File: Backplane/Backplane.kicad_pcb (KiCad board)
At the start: 4 copper layers, 101.6 x 120.6 mm, 40 parts, among them J10 Conn_01x02, J11 Conn_01x02, J12 Conn_02x12_Odd_Even, J13 Conn_01x02, J14 Conn_01x02, J15 Conn_01x02, J16 Conn_01x02, J17 Conn_01x02, J18 Conn_01x02, J19 Conn_01x02_Pin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

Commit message: Changed Backplane and Power Card for proper connection between the killswitches in the new system
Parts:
- added NJKS: Conn_01x02, Connector_JST:JST_PH_B2B-PH-K_1x02_P2.00mm_Vertical, F.Cu at (74.0, 137.0)
- J27: renamed from Power (+12V)
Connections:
- J1 pad A27: SW2 -> unconnected-(J1-PadA27)
- J1 pad A28: GND -> unconnected-(J1-PadA28)
- J1 pad B27: SW2 -> SW
- J1 pad B28: SW1 -> NJSW
- J1 pad C27: GND -> SW
- J1 pad C28: SW1 -> NJSW
- J9 pad 1: SW2 -> SW
- J9 pad 2: SW1 -> GND
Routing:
- net SW1: track 166.3 -> 0.00 mm, vias 1 -> 0
- net SW2: track 159.0 -> 0.00 mm, vias 1 -> 0
- net SW: track 0.00 -> 156.5 mm, vias 0 -> 1
- net NJSW: track 0.00 -> 155.3 mm, vias 0 -> 1

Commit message: Added short on power card and fixed some connections
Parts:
- renumbered J27 to 12V
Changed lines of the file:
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@@
 		(descr "JST PH series connector, B2B-PH-K (http://www.jst-mfg.com/product/pdf/eng/ePH.pdf), generated with kicad-footprint-generator")
 		(tags "connector JST PH vertical")
-		(property "Reference" "J27"
-			(at -2.5 -3 90)
+		(property "Reference" "12V"
+			(at -3 -2.5 90)
 			(layer "F.SilkS")
 			(effects
@@
 			(layer "F.Fab")
 		)
-		(fp_text user "${REFERENCE}"
-			(at 1 1.5 90)
-			(layer "F.Fab")
-			(effects
-				(font
-					(size 1 1)
-					(thickness 0.15)
-				)
-			)
-		)
 		(pad "1" thru_hole roundrect
 			(at 0 0 90)
@@
 			(layer "F.Fab")
 		)
-		(fp_text user "${REFERENCE}"
-			(at 1 1.5 90)
-			(layer "F.Fab")
-			(effects
-				(font
-					(size 1 1)
-					(thickness 0.15)
-				)
-			)
-		)
 		(pad "1" thru_hole roundrect

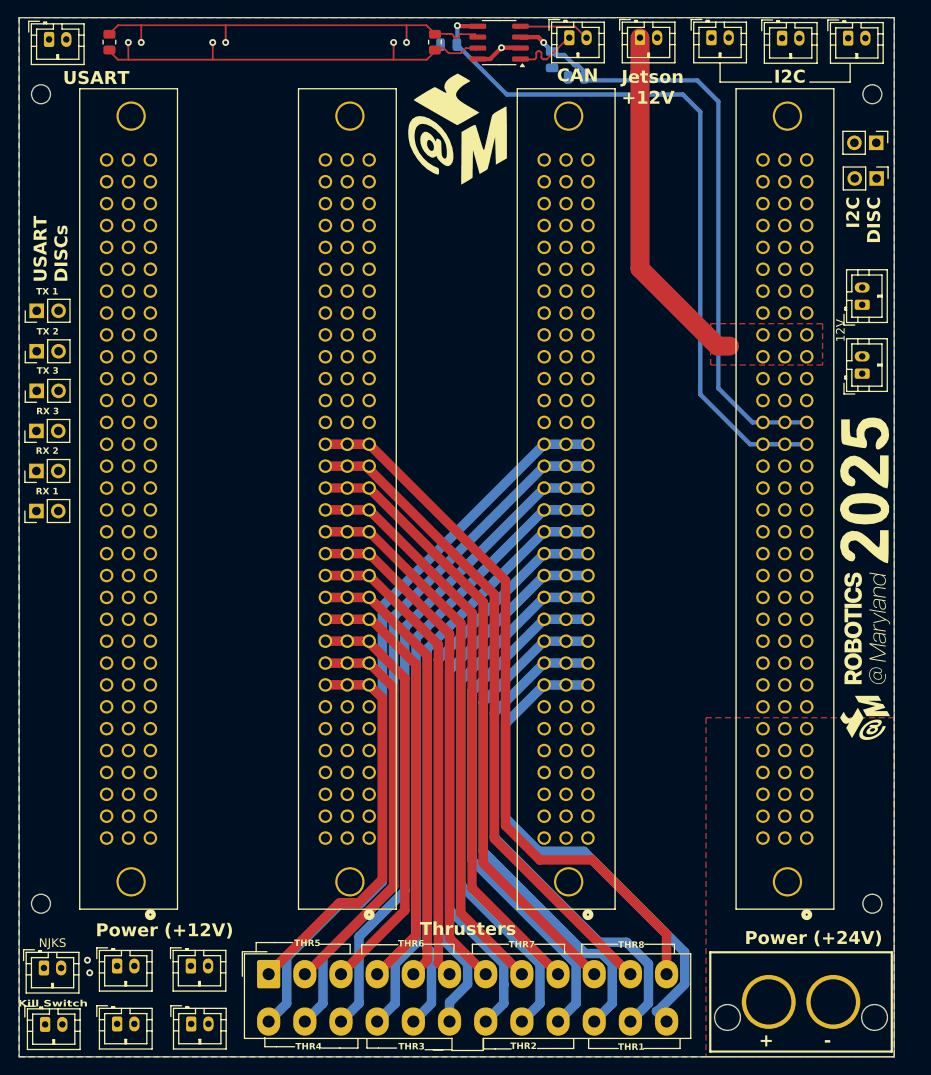
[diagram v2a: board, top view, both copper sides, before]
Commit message: Added Silkscreen & Backplane Integration
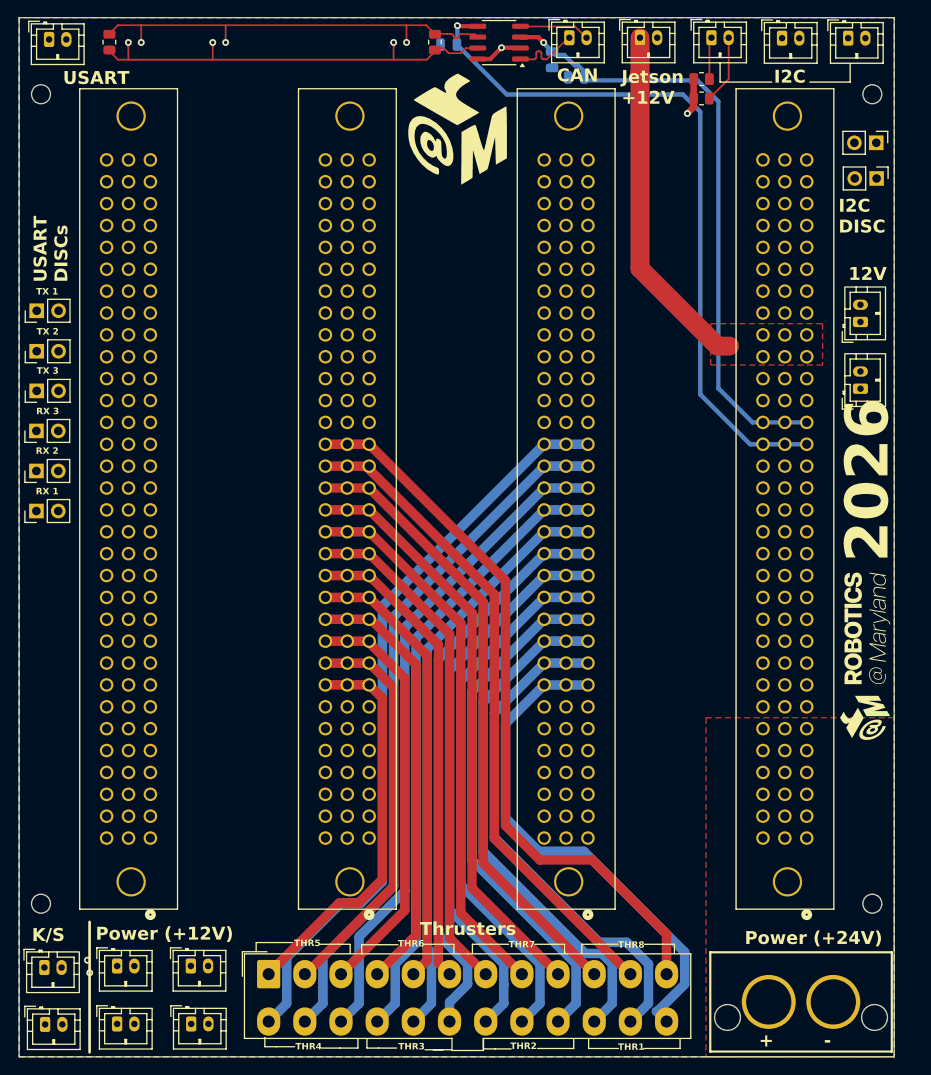
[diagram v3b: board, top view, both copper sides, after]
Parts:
- removed 12V, NJKS: Conn_01x02, Connector_JST:JST_PH_B2B-PH-K_1x02_P2.00mm_Vertical
- removed the G*** at (169.4, 81.5)
- added J27: Conn_01x02, Connector_JST:JST_PH_B2B-PH-K_1x02_P2.00mm_Vertical, F.Cu at (168.8, 69.8)
- added J28: Conn_01x02, Connector_JST:JST_PH_B2B-PH-K_1x02_P2.00mm_Vertical, F.Cu at (74.0, 136.9)
- added R3: 4.7k, Resistor_SMD:R_0805_2012Metric, F.Cu at (150.3, 33.8)
- added R4: 4.7k, Resistor_SMD:R_0805_2012Metric, F.Cu at (150.3, 36.0)
- moved J15 6.00 mm to (168.8, 62.0)
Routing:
- net +3.3V: track 0.00 -> 34.1 mm, vias 0 -> 1
- net I2CJetson-: track 45.6 -> 53.5 mm
- net I2CJetson+: track 45.6 -> 50.5 mm
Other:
- board text added: "12V"
- board text added: "2026"
- board text added: "K/S"
- board text removed: "Kill Switch"

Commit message: Kurt Changes
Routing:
- net +3.3V: track 34.1 -> 37.9 mm
- net 12V Jetson: track 40.9 -> 42.8 mm
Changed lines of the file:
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@@
+	)
+	(segment
+		(start 146.7 39.8)
+		(end 149.4375 37.0625)
+		(width 0.75)
+		(layer "F.Cu")
+		(net 5)
+	)
+	(segment
+		(start 146.7 59)
+		(end 146.7 39.8)
+		(width 0.75)
+		(layer "F.Cu")
+		(net 5)
 	)
 	(segment
@@
 	(segment
 		(start 149.4375 37.0625)
-		(end 148.7 37.8)
+		(end 149.4375 36.05)
 		(width 0.75)
 		(layer "F.Cu")
 		(net 5)
 	)
-	(segment
-		(start 149.4375 36.05)
-		(end 149.4375 37.0625)
-		(width 0.75)
-		(layer "F.Cu")
-		(net 5)
-	)
 	(via
-		(at 148.7 37.8)
+		(at 146.7 59)
 		(size 0.8)
 		(drill 0.4)
@@
 	)
 	(segment
-		(start 148.7 37.8)
-		(end 148.7 67.55)
+		(start 146.7 59)
+		(end 146.7 70.6)
 		(width 0.75)
 		(layer "In1.Cu")
@@
 	)
 	(segment
-		(start 143.2 55.8)
-		(end 151.6 64.2)
-		(width 2.2)
-		(layer "F.Cu")
-		(net 16)
-	)
-	(segment
-		(start 152.2 64.8)
+		(start 149 64.8)
 		(end 153.6 64.8)
 		(width 2.2)
@@
 	)
 	(segment
-		(start 151.6 64.2)
-		(end 152.2 64.8)
+		(start 143.2 29)
+		(end 143.2 59)
 		(width 2.2)
 		(layer "F.Cu")
@@
 	)
 	(segment
-		(start 143.2 29)
-		(end 143.2 33)
+		(start 143.2 59)
+		(end 149 64.8)
 		(width 2.2)
 		(layer "F.Cu")
-		(net 16)
-	)
-	(segment
-		(start 143.2 33)
-		(end 143.2 55.8)
-		(width 2.2)
-		(layer "F.Cu")

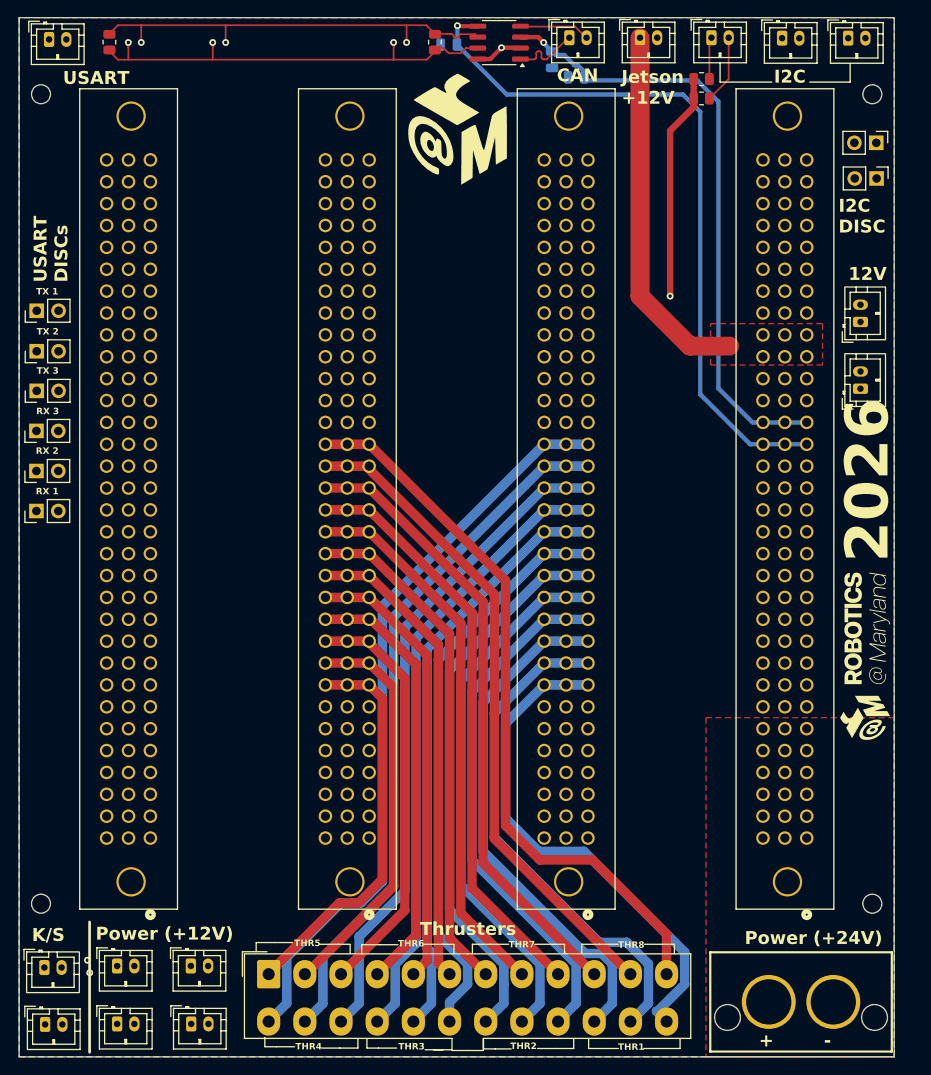
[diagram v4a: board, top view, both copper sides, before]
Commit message: Added More Connectors to Backplane
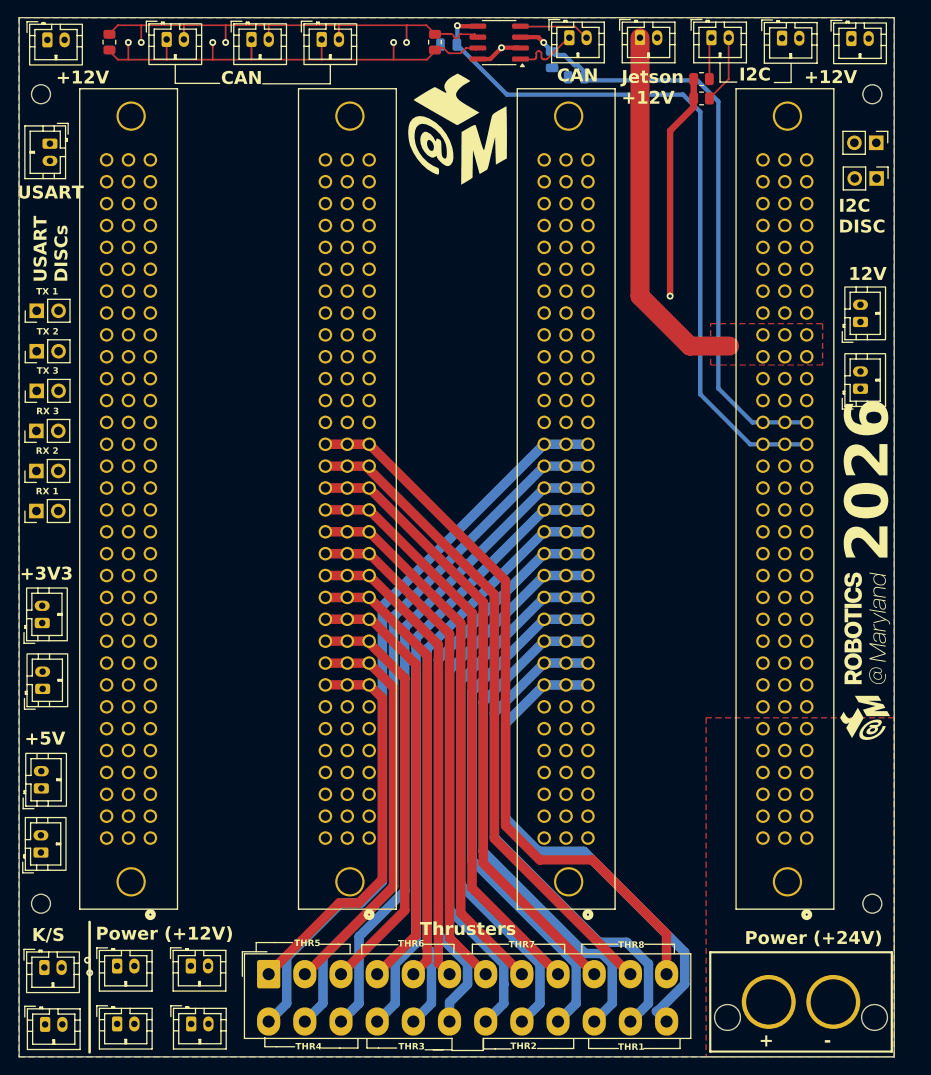
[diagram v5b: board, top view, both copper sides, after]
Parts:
- removed J16: Conn_01x02, Connector_JST:JST_PH_B2B-PH-K_1x02_P2.00mm_Vertical
- added J29: Conn_01x02, Connector_JST:JST_PH_B2B-PH-K_1x02_P2.00mm_Vertical, F.Cu at (88.2, 29.2)
- added J30: Conn_01x02, Connector_JST:JST_PH_B2B-PH-K_1x02_P2.00mm_Vertical, F.Cu at (98.1, 29.2)
- added J31: Conn_01x02, Connector_JST:JST_PH_B2B-PH-K_1x02_P2.00mm_Vertical, F.Cu at (73.8, 104.6)
- added J32: Conn_01x02, Connector_JST:JST_PH_B2B-PH-K_1x02_P2.00mm_Vertical, F.Cu at (73.8, 97.0)
- added J33: Conn_01x02, Connector_JST:JST_PH_B2B-PH-K_1x02_P2.00mm_Vertical, F.Cu at (73.7, 116.2)
- added J34: Conn_01x02, Connector_JST:JST_PH_B2B-PH-K_1x02_P2.00mm_Vertical, F.Cu at (73.7, 123.6)
- added J35: Conn_01x02, Connector_JST:JST_PH_B2B-PH-K_1x02_P2.00mm_Vertical, F.Cu at (106.2, 29.2)
- added J36: Conn_01x02, Connector_JST:JST_PH_B2B-PH-K_1x02_P2.00mm_Vertical, F.Cu at (74.4, 29.2)
- added J37: Conn_01x02, Connector_JST:JST_PH_B2B-PH-K_1x02_P2.00mm_Vertical, F.Cu at (167.8, 29.1)
- moved J18 12.1 mm to (74.7, 41.3), turned to -90 degrees
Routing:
- net USART+: track 56.5 -> 30.2 mm
- net I2CJetson+: track 50.5 -> 33.0 mm
- net I2CJetson-: track 53.5 -> 40.2 mm
- net CAN+: track 169.6 -> 176.6 mm
- net CAN-: track 165.2 -> 170.1 mm
- added copper zone on In2.Cu, net +3.3V
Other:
- board text added: "+12V"
- board text added: "+3V3"
- board text added: "+5V"

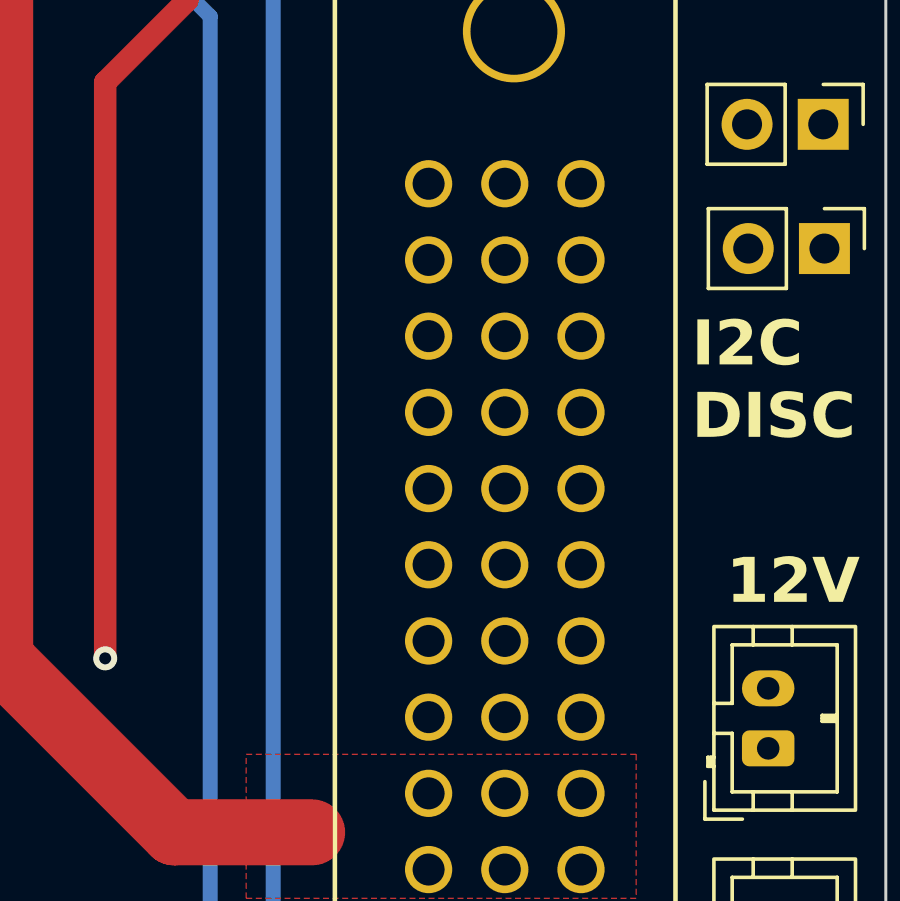
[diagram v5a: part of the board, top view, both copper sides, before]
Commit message: Moved I2C Pins for Power Card
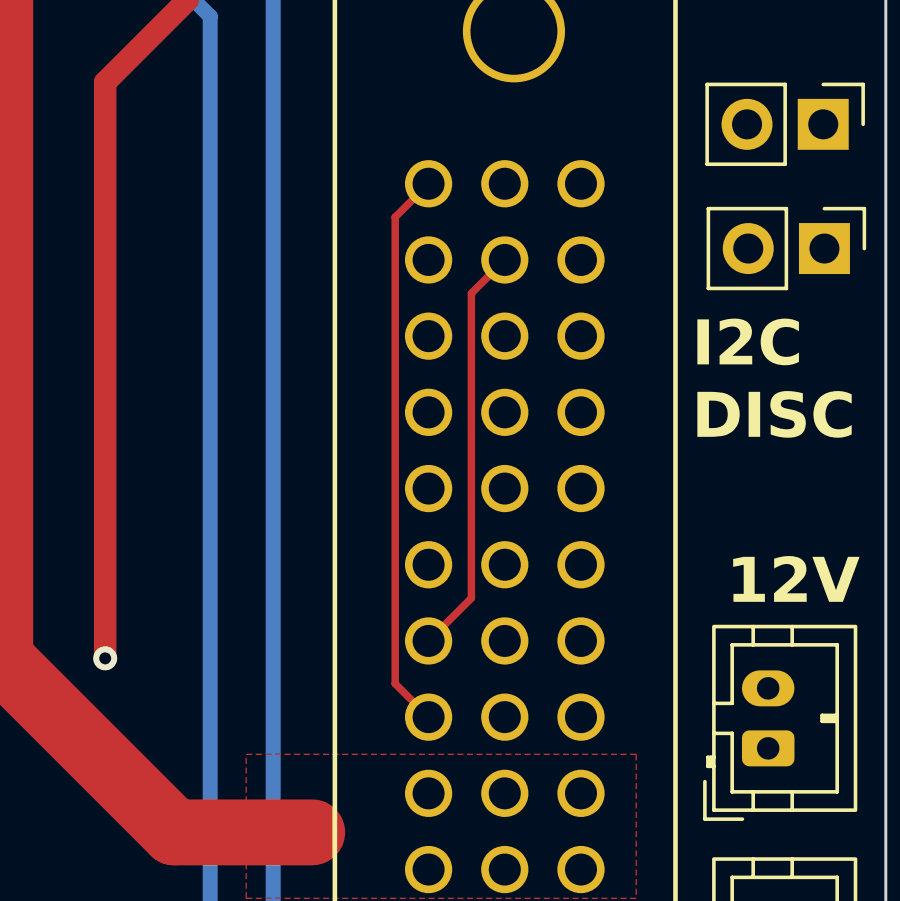
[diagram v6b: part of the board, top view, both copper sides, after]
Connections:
- J1 pad C25: unconnected-(J1-PadC25) -> I2C+
- J1 pad C26: unconnected-(J1-PadC26) -> I2C-
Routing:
- net I2C+: track 90.4 -> 109.1 mm
- net I2C-: track 87.6 -> 101.4 mm
